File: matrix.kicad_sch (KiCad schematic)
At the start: 129 parts

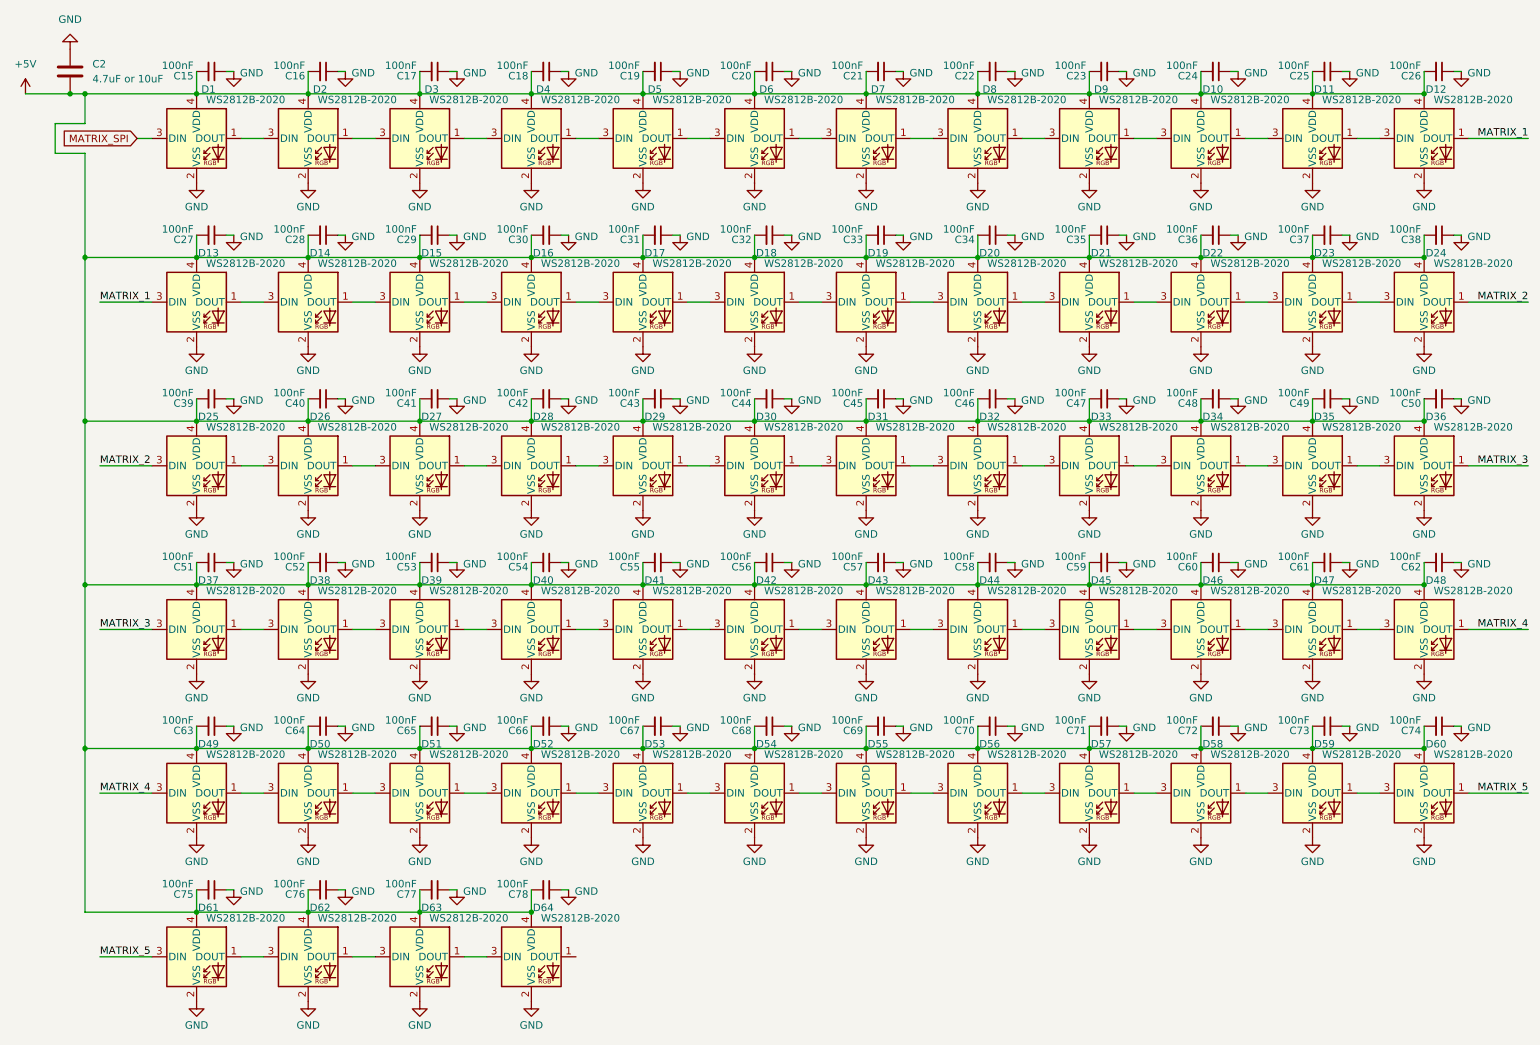
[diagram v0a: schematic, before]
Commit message: Remove unneeded capacitors from LED matrix
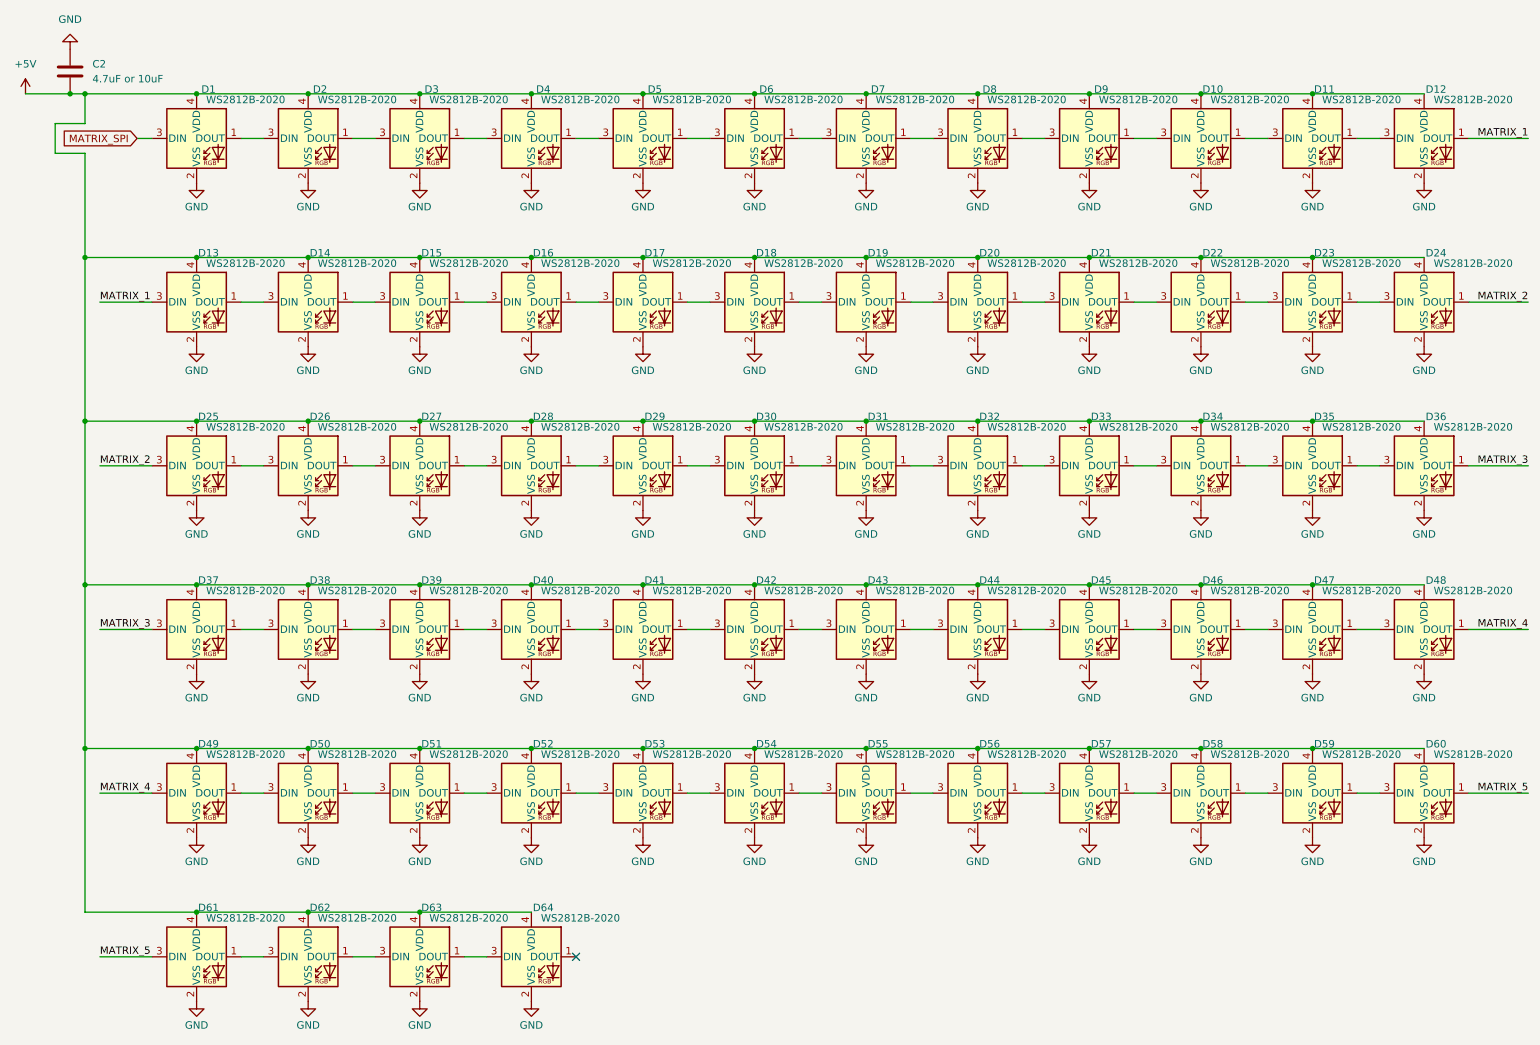
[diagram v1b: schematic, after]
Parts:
- removed C15, C16, C17, C18, C19, C20, C21, C22, C23, C24, C25, C26, C27, C28, C29, C30, C31, C32, C33, C34, C35, C36, C37, C38, C39, C40, C41, C42, C43, C44, C45, C46, C47, C48, C49, C50, C51, C52, C53, C54, C55, C56, C57, C58, C59, C60, C61, C62, C63, C64, C65, C66, C67, C68, C69, C70, C71, C72, C73, C74, C75, C76, C77, C78: 100nF, Capacitor_SMD:C_0402_1005Metric, symbol Device:C_Small
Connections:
- no-connect marks 0 -> 1
